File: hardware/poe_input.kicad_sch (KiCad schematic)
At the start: 3 parts, among them M1 DP9900LPB-5V1.4A

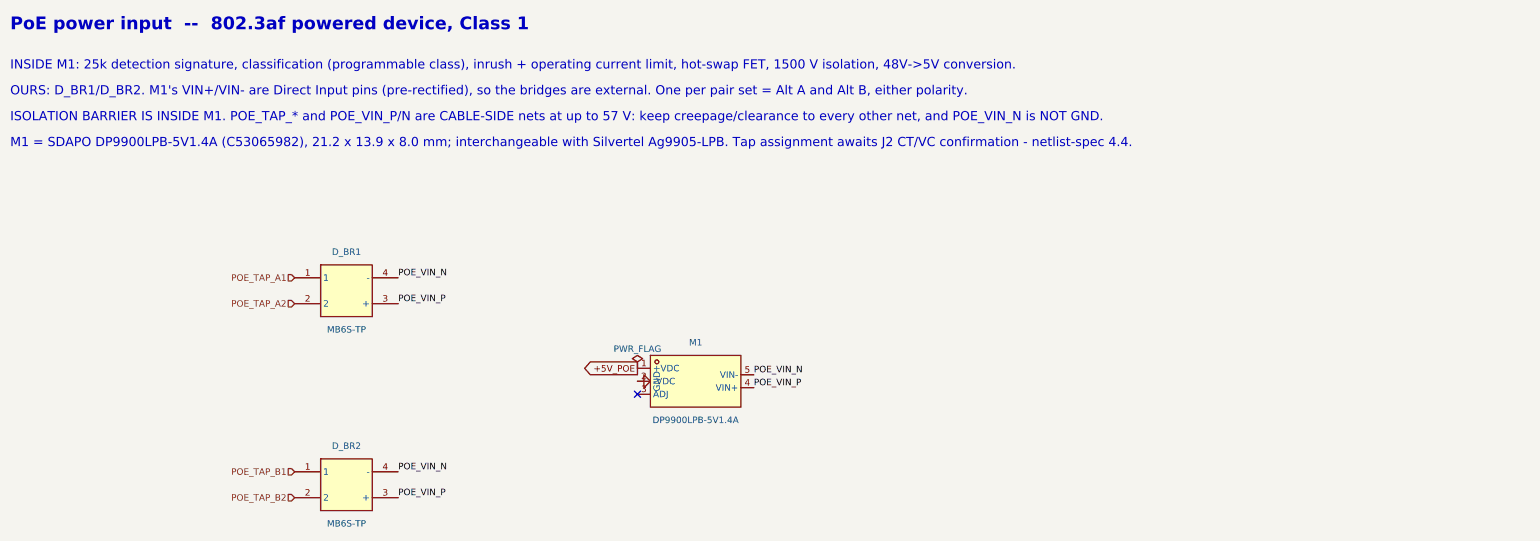
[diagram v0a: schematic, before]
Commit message: hardware: updated board design (reference renumbering, LED polarity fix, crystal symbol upgrade)
Replaces the schematics/PCB/project file with the latest design. Key
changes, verified before committing (netlist-check.py: 124 checks, 0
failures; ERC unchanged at 3 known pin_not_driven findings on W5500 SPI
inputs, same severity-policy artifact as before):

- Component reference designators changed from descriptive names
  (R_ATN, C_3V3, D_BR1, etc.) to plain auto-numbered ones (R15, C9, D1,
  etc.) -- intentional, since descriptive names were ending up on the
  silkscreen; they belong in the BOM instead. docs/netlist-spec.nets
  updated to match via a UUID-verified old-ref -> new-ref mapping (every
  renamed symbol's KiCad UUID was unchanged, confirming these are pure
  renames with no electrical difference), not a hand transcription.
- LED1's wiring was corrected: the old schematic had its anode tied to
  GND and cathode driven by LED_A (backwards -- confirmed via each net's
  pinfunction annotation in the exported netlist, K_1/A_2, which is
  fixed by the Device:LED symbol regardless of reference numbering).
  The new schematic has cathode-to-GND, anode-to-LED_A, the correct
  orientation.
- X1/X2 changed from Device:Crystal (2-pin) to Device:Crystal_GND24
  (4-pin, case-ground on pins 2/4) -- a more accurate symbol for the
  real SMD crystal package. netlist-spec.nets updated accordingly
  (XOUT/ETH_XO now reference pin 3, GND gained the four case pins).

mcu.kicad_sch was supplied separately (missing from the first archive);
confirmed it has no further sub-sheet references and all its symbols'
footprint names resolve against the existing hardware/lib/adapter.pretty/
library, which was deliberately left untouched along with fp-lib-table,
sym-lib-table, and .konnect/ -- none of those changed in this update.
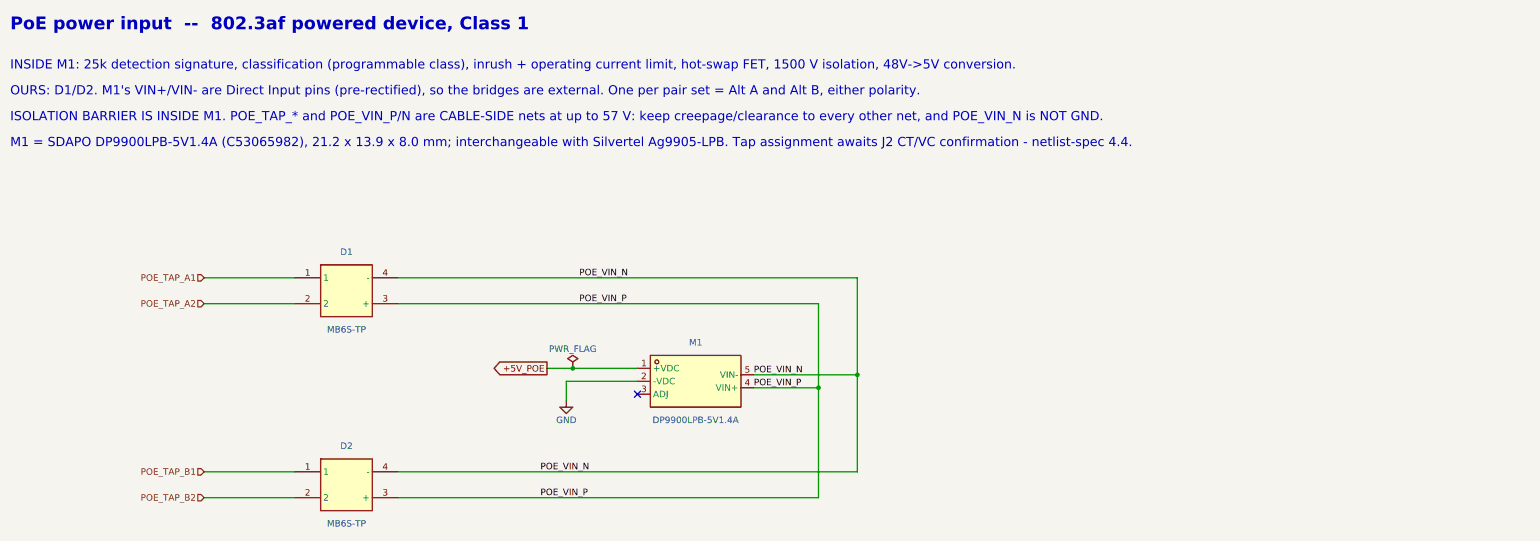
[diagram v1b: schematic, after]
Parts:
- D1: renamed from D_BR1; LCSC (none) -> C85619
- D2: renamed from D_BR2; LCSC (none) -> C85619
- M1: LCSC (none) -> C53065982
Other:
- note added: "OURS: D1/D2. M1's VIN+/VIN- are Direct Input pins (pre-rectified), so the bridges are external. One per pair set = Alt A and Alt B, either polarity."
- note removed: "OURS: D_BR1/D_BR2. M1's VIN+/VIN- are Direct Input pins (pre-rectified), so the bridges are external. One per pair set = Alt A and Alt B, either polarity."
